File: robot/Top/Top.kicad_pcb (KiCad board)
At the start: 2 copper layers, 0 parts

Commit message: Top PCB
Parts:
- added C2: 10µ, Capacitors_SMD:C_1206, B.Cu at (134.2, 120.2)
- added C3: 1µ, Capacitors_SMD:C_1206, B.Cu at (172.0, 111.8)
- added C4: 1µ, Capacitors_SMD:C_1206, B.Cu at (172.0, 106.5)
- added C5: 1µ, Capacitors_SMD:C_1206, B.Cu at (172.0, 101.2)
- added C6: 4.7µ, Capacitors_SMD:C_1206, B.Cu at (165.0, 98.9)
- added C7: 4.7µ, Capacitors_SMD:C_1206, B.Cu at (168.4, 100.0)
- added D1: D_Schottky, Diodes_SMD:D_SOD-123, B.Cu at (150.5, 97.5)
- added D2: ORANGE, LEDs:LED_0603, B.Cu at (135.0, 109.8)
- added H1: BAT_MON, Custom:Mounting_Pad_Signal, B.Cu at (140.0, 94.5)
- added H10: GND, Custom:Mounting_Pad_Power, B.Cu at (129.2, 95.0)
- added H2: VBAT_SWITCH, Custom:Mounting_Pad_Power, B.Cu at (168.2, 95.0)
- added H3: OLED_~RES, Custom:Mounting_Pad_Signal, B.Cu at (164.5, 94.5)
- added H4: OLED_SCL, Custom:Mounting_Pad_Signal, B.Cu at (162.0, 94.5)
- added H5: OLED_SDA, Custom:Mounting_Pad_Signal, B.Cu at (159.5, 94.5)
- added H6: VBUS, Custom:Mounting_Pad_Power, B.Cu at (136.2, 95.0)
- added H7: 3V3, Custom:Mounting_Pad_Power, B.Cu at (132.8, 95.0)
- added H8: GND, Custom:Mounting_Pad_Power, B.Cu at (171.8, 95.0)
- added J1: Conn_01x02_Male, Custom:Conn_Bat, B.Cu at (131.0, 126.3)
- added R1: 100K, Resistors_SMD:R_1206, B.Cu at (129.6, 119.2)
- added R2: 100K, Resistors_SMD:R_1206, B.Cu at (129.6, 113.5)
- added R3: 1K, Resistors_SMD:R_1206, B.Cu at (130.7, 109.8)
- added R4: 5K, Resistors_SMD:R_1206, B.Cu at (138.9, 116.5)
- added R5: 330k, Resistors_SMD:R_1206, B.Cu at (165.1, 112.2)
- added SW1: SW_DPDT_x2, Custom:JS102011SAQN, B.Cu at (134.1, 103.8)
- added U2: MCP73831-2-OT, Package_TO_SOT_SMD:SOT-23-5, B.Cu at (134.2, 116.5)
- added U3: SSD1306, Custom:SSD1306_OLED, B.Cu at (165.2, 110.0)
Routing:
- net +3V3: track 0.00 -> 61.6 mm, vias 0 -> 2
- net /BAT_MON: track 0.00 -> 32.1 mm, vias 0 -> 2
- net +BATT: track 0.00 -> 29.3 mm, vias 0 -> 2
- net VBUS: track 0.00 -> 24.2 mm
- net /VBAT_SWITCH: track 0.00 -> 18.3 mm, vias 0 -> 2
- net Net-(D1-Pad2): track 0.00 -> 17.4 mm, vias 0 -> 2
- net /OLED_~RES: track 0.00 -> 14.9 mm
- net /OLED_SDA: track 0.00 -> 13.2 mm, vias 0 -> 2
- net /OLED_SCL: track 0.00 -> 12.6 mm, vias 0 -> 2
- net Net-(R5-Pad2): track 0.00 -> 12.5 mm, vias 0 -> 2
- net Net-(R3-Pad2): track 0.00 -> 12.2 mm
- net Net-(C6-Pad1): track 0.00 -> 9.27 mm, vias 0 -> 2
- net Net-(C3-Pad1): track 0.00 -> 8.20 mm
- net Net-(C4-Pad2): track 0.00 -> 8.15 mm
- net Net-(C3-Pad2): track 0.00 -> 7.21 mm
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- added copper zone on B.Cu, net GND
- added copper zone on F.Cu, net GND
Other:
- board outline added: 46 x 46 mm
- net class Power added: clearance 0.3, trace_width 0.5, via_dia 1, via_drill 0.5

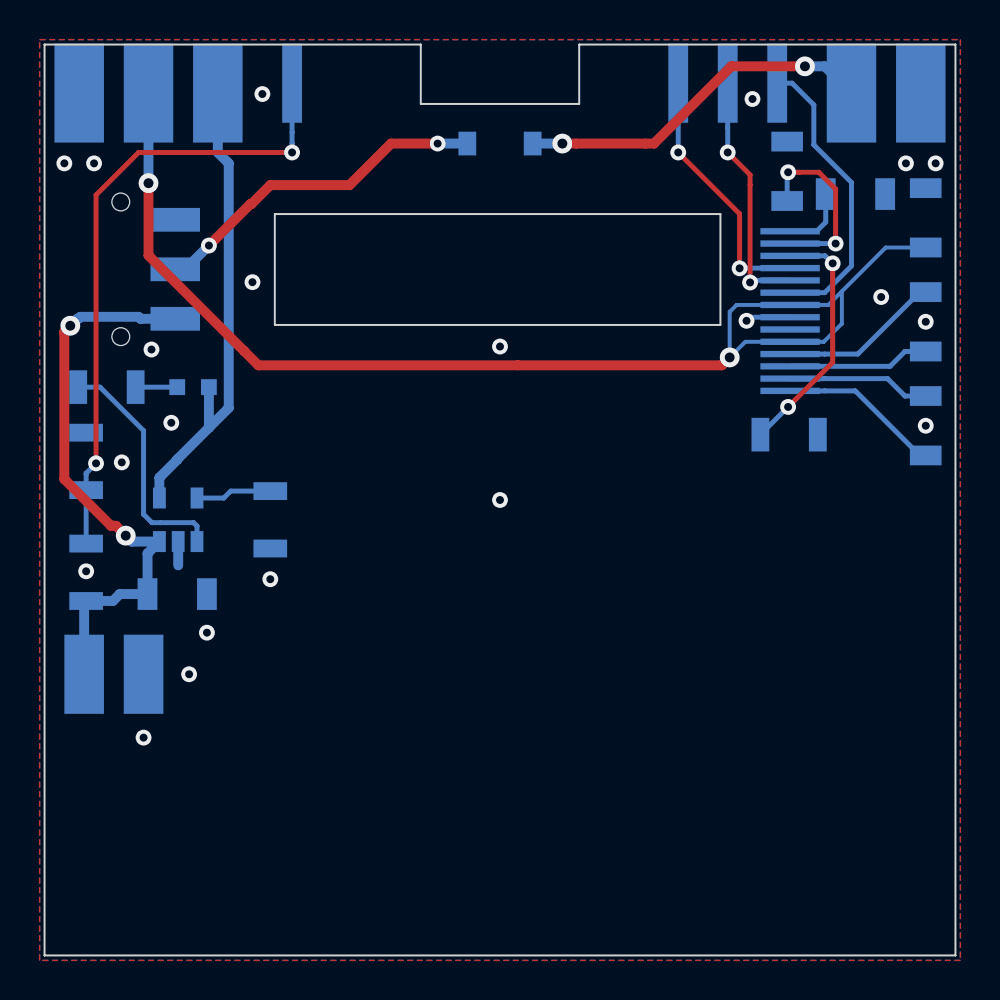
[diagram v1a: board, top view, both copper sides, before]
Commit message: Swap 3V3 and VBUS, Fix Cutout, small changes
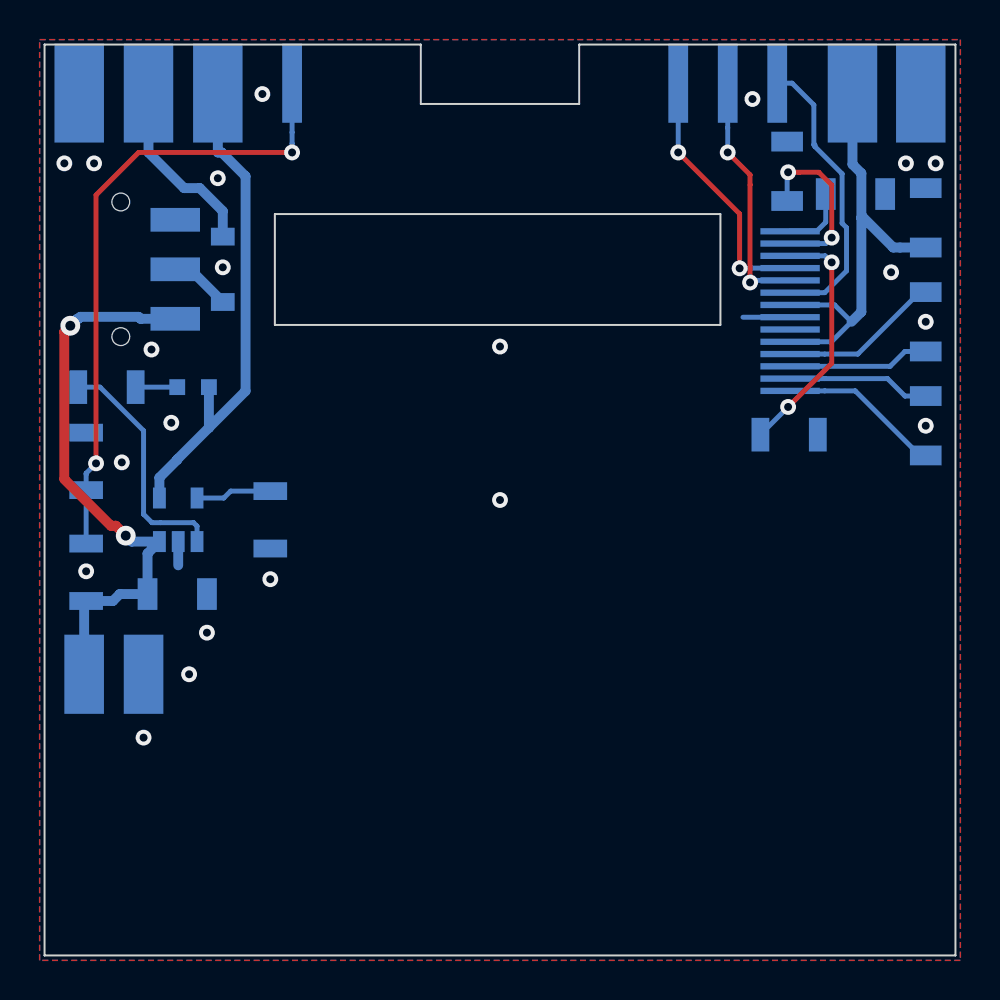
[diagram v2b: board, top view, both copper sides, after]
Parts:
- moved H7 35.6 mm to (168.3, 95.0)
- moved H2 35.5 mm to (132.8, 95.0)
- moved D1 15.4 mm to (136.5, 103.8), turned to 270 degrees
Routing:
- net +3V3: track 61.6 -> 22.8 mm, vias 2 -> 0
- net Net-(D1-Pad2): track 17.4 -> 4.03 mm, vias 2 -> 0
- net /VBAT_SWITCH: track 18.3 -> 9.27 mm, vias 2 -> 0
- net VBUS: track 24.2 -> 25.0 mm

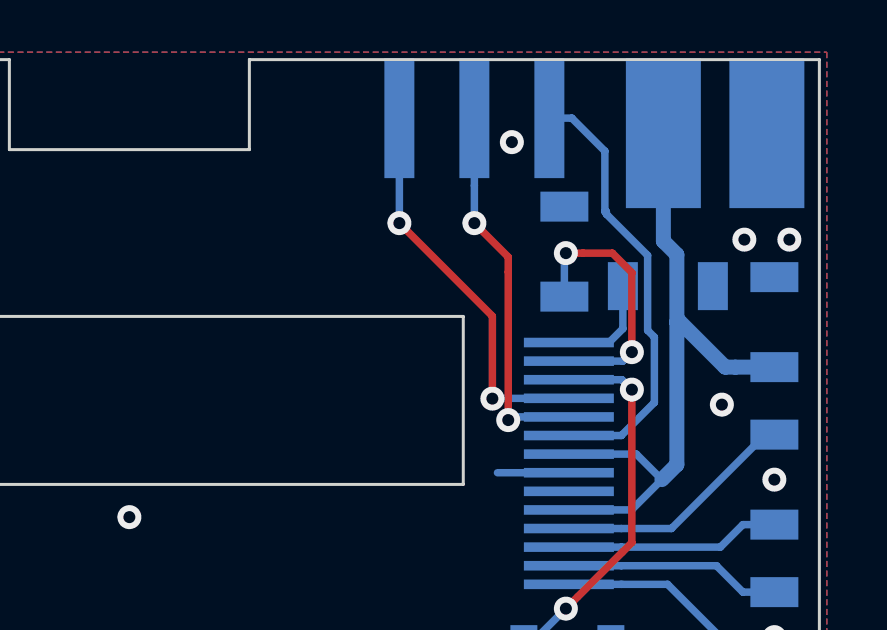
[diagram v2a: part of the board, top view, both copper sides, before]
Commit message: Silkscreen Top
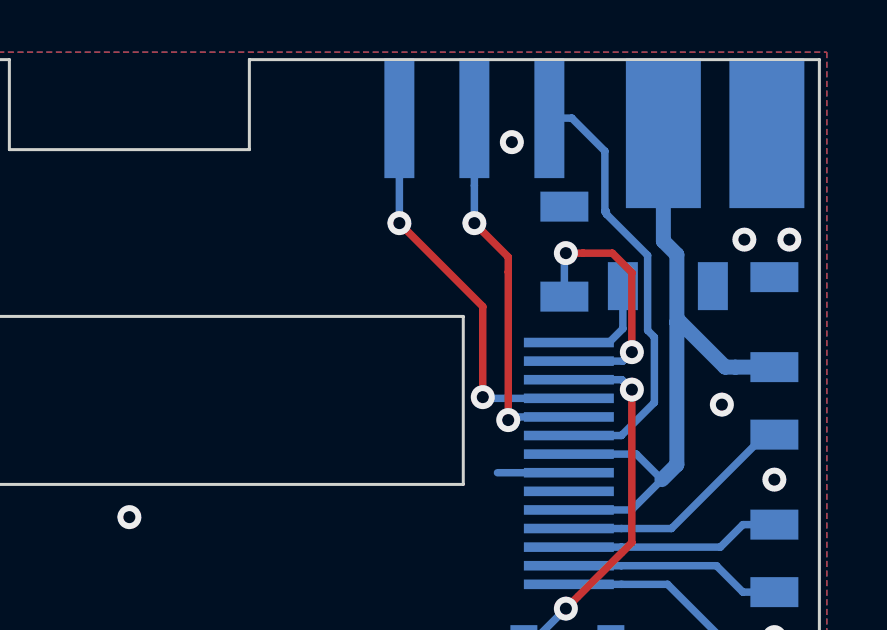
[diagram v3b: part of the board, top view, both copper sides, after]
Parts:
- H2: value VBAT_SWITCH -> VBS
- H3: value OLED_~RES -> ORST
- H4: value OLED_SCL -> OSCL
- H5: value OLED_SDA -> OSDA

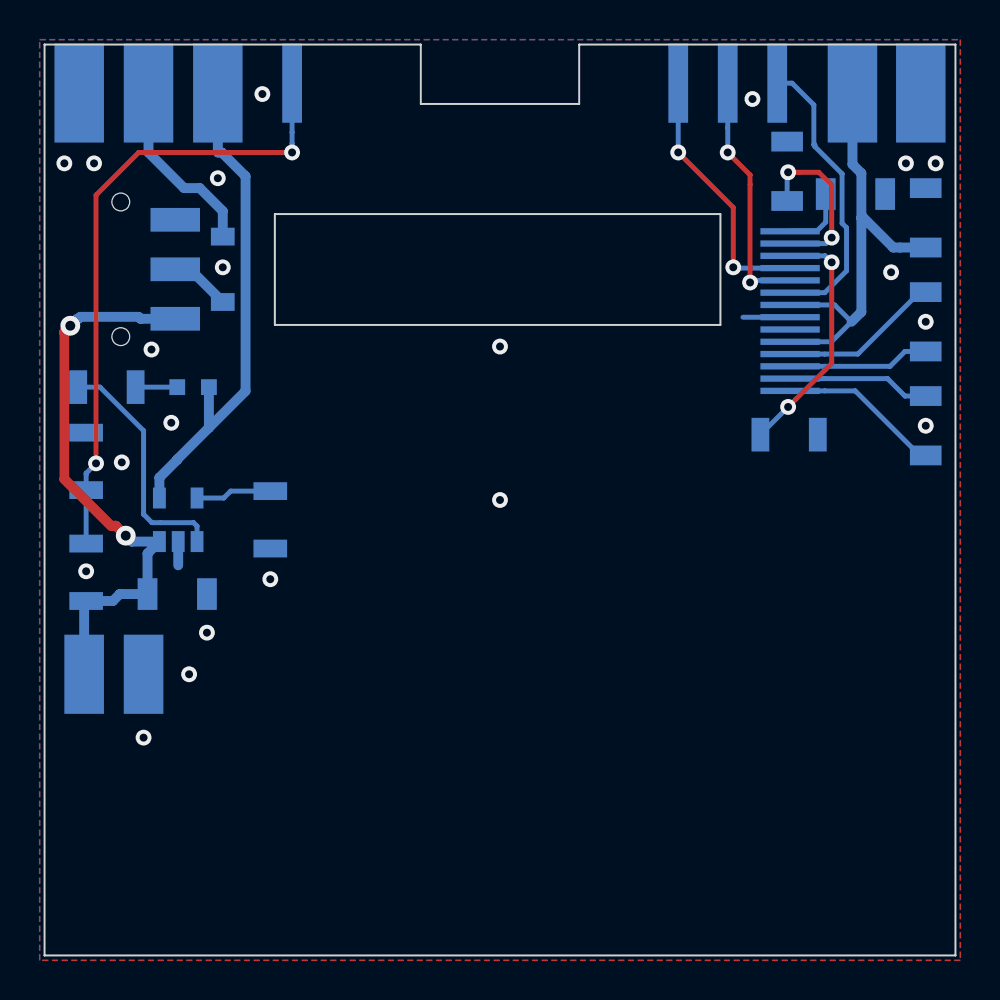
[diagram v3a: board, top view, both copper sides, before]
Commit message: Finish Top, remap OLED pins
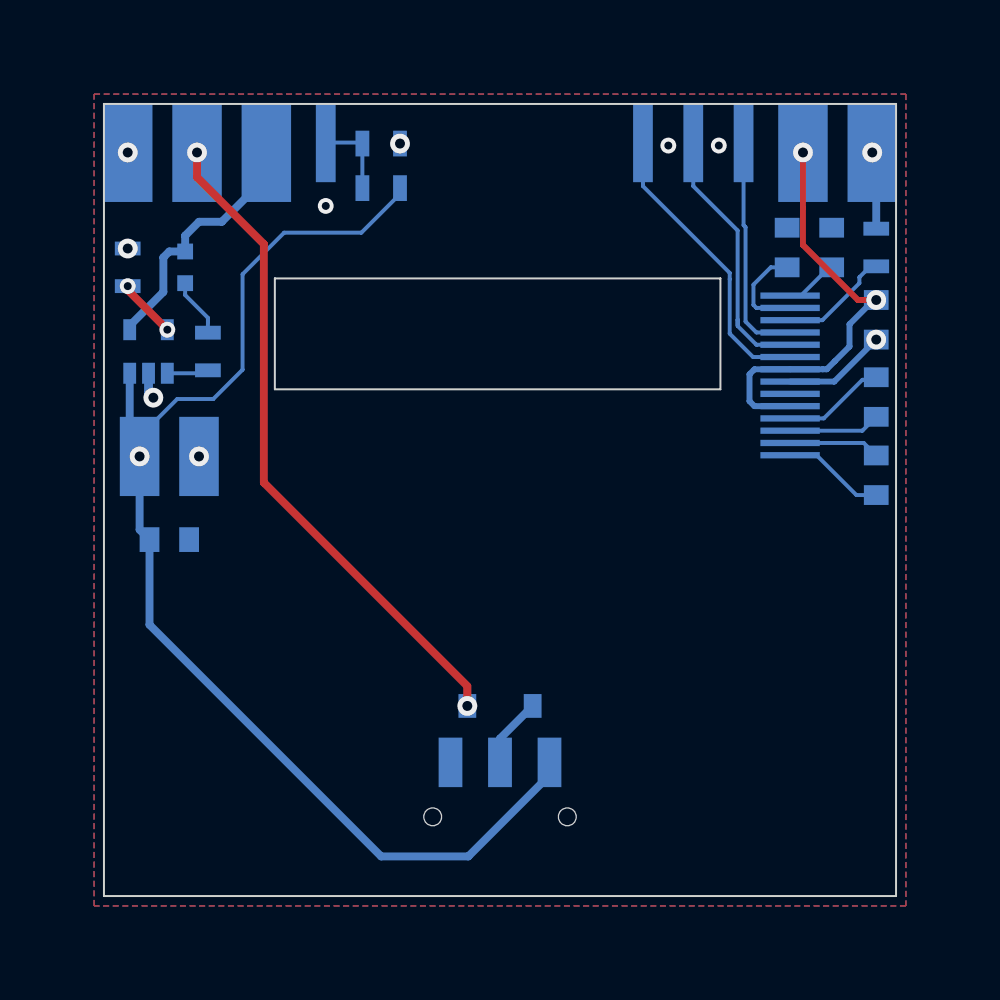
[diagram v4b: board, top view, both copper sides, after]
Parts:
- C2, C3, C4, C5, C6, C7: footprint Capacitors_SMD:C_1206 -> Capacitors_SMD:C_0805
- H1: value BAT_MON -> BTMN
- R1, R2, R3, R4, R5: footprint Resistors_SMD:R_1206 -> Resistors_SMD:R_0805
- moved SW1 29.8 mm to (150.5, 128.8), turned to 180 degrees
- moved D1 26.1 mm to (150.5, 125.9), turned to 0 degrees
- moved R1 24.5 mm to (144.5, 99.8), turned to 180 degrees
- moved R2 21.9 mm to (144.5, 97.5), turned to 0 degrees
- moved R4 14.6 mm to (131.7, 103.8), turned to 90 degrees
- moved J1 11.4 mm to (133.8, 115.3)
- moved R5 10.4 mm to (169.5, 102.8), turned to 270 degrees
- moved U2 8.63 mm to (132.8, 108.0)
- moved H3 7.41 mm to (157.7, 97.5)
- moved D2 6.06 mm to (134.6, 103.8), turned to 90 degrees
- moved C5 5.72 mm to (169.5, 106.4), turned to 270 degrees
- moved R3 5.41 mm to (135.8, 108.0), turned to 270 degrees
- moved C4 4.55 mm to (169.5, 110.3)
- moved H5 4.46 mm to (162.8, 97.5)
- moved H7 3.91 mm to (165.8, 98.0)
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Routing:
- net +BATT: track 29.3 -> 62.9 mm, vias 2 -> 1
- net /BAT_MON: track 32.1 -> 4.12 mm, vias 2 -> 0
- net /VBAT_SWITCH: track 9.27 -> 33.6 mm, vias 0 -> 2
- net VBUS: track 25.0 -> 14.7 mm
- net Net-(R3-Pad2): track 12.2 -> 2.11 mm
- net GND: track 3.58 -> 11.6 mm, vias 21 -> 10
- net Net-(R5-Pad2): track 12.4 -> 5.65 mm, vias 2 -> 0
- net Net-(C6-Pad1): track 8.81 -> 5.00 mm, vias 2 -> 0
- net Net-(C3-Pad1): track 8.20 -> 5.18 mm
- net Net-(C4-Pad2): track 8.15 -> 5.21 mm
- net Net-(C3-Pad2): track 7.21 -> 4.61 mm
- net Net-(C4-Pad1): track 7.16 -> 4.64 mm
- net /OLED_~RES: track 14.7 -> 16.5 mm
- net /OLED_SDA: track 13.4 -> 11.6 mm, vias 2 -> 0
- net +3V3: track 22.8 -> 21.7 mm, vias 0 -> 2
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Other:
- board size 46 x 46 mm -> 40 x 40 mm
- net class Default: trace_width 0.25 -> 0.2
- net class Power: trace_width 0.5 -> 0.4

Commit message: Small fixes, step files
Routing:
- net +BATT: track 62.9 -> 62.3 mm, vias 1 -> 0
- net /VBAT_SWITCH: track 33.6 -> 34.1 mm, vias 2 -> 3
- net GND: vias 10 -> 11
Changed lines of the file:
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@@
     (thickness 1.6)
     (drawings 13)
-    (tracks 130)
+    (tracks 137)
     (zones 0)
     (modules 26)
@@
   (via (at 161.55 97.6) (size 0.8) (drill 0.4) (layers F.Cu B.Cu) (net 1))
   (via (at 141.7 100.65) (size 0.8) (drill 0.4) (layers F.Cu B.Cu) (net 1))
+  (via (at 150.5 115.5) (size 1) (drill 0.5) (layers F.Cu B.Cu) (net 1))
   (segment (start 145.45 100.05) (end 145.45 99.75) (width 0.2) (layer B.Cu) (net 2))
   (segment (start 131.8 112.8) (end 132.3 113.3) (width 0.4) (layer B.Cu) (net 2))
@@
   (segment (start 144.5 133.5) (end 148.9 133.5) (width 0.4) (layer B.Cu) (net 2))
   (segment (start 132.3 113.3) (end 132.3 112.3) (width 0.2) (layer B.Cu) (net 2))
-  (segment (start 132.3 112.3) (end 134.2 110.4) (width 0.2) (layer B.Cu) (net 2))
-  (segment (start 137.5 104.1) (end 139.6 102) (width 0.2) (layer B.Cu) (net 2))
-  (segment (start 134.2 110.4) (end 136.020002 110.4) (width 0.2) (layer B.Cu) (net 2))
-  (segment (start 136.020002 110.4) (end 137.5 108.920002) (width 0.2) (layer B.Cu) (net 2))
-  (segment (start 137.5 108.920002) (end 137.5 104.1) (width 0.2) (layer B.Cu) (net 2))
-  (via (at 132.3 113.3) (size 1) (drill 0.5) (layers F.Cu B.Cu) (net 2))
-  (segment (start 139.6 102) (end 143.5 102) (width 0.2) (layer B.Cu) (net 2))
   (segment (start 143.5 102) (end 145.45 100.05) (width 0.2) (layer B.Cu) (net 2))
+  (segment (start 143.5 102) (end 137.95 102) (width 0.2) (layer B.Cu) (net 2))
+  (segment (start 137.95 102) (end 136.85001 103.09999) (width 0.2) (layer B.Cu) (net 2))
+  (segment (start 136.85001 107.669992) (end 136.420002 108.1) (width 0.2) (layer B.Cu) (net 2))
+  (segment (start 136.85001 103.09999) (end 136.85001 107.669992) (width 0.2) (layer B.Cu) (net 2))
+  (segment (start 131.8 108.37) (end 131.8 109.1) (width 0.2) (layer B.Cu) (net 2))
+  (segment (start 132.07 108.1) (end 131.8 108.37) (width 0.2) (layer B.Cu) (net 2))
+  (segment (start 136.420002 108.1) (end 132.07 108.1) (width 0.2) (layer B.Cu) (net 2))
   (segment (start 168.5 115.25) (end 169.5 115.25) (width 0.2) (layer B.Cu) (net 3))
   (segment (start 165.15 113.24) (end 166.49 113.24) (width 0.2) (layer B.Cu) (net 3))
@@
   (segment (start 168.87 112.62) (end 169.5 113.25) (width 0.2) (layer B.Cu) (net 4))
   (segment (start 165.15 112.62) (end 168.87 112.62) (width 0.2) (layer B.Cu) (net 4))
-  (segment (start 166.85 111.38) (end 168.8 109.43) (width 0.2) (layer B.Cu) (net 5))
-  (segment (start 165.15 111.38) (end 166.85 111.38) (width 0.2) (layer B.Cu) (net 5))
-  (segment (start 169.37 109.43) (end 169.5 109.3) (width 0.2) (layer B.Cu) (net 5))
-  (segment (start 168.8 109.43) (end 169.37 109.43) (width 0.2) (layer B.Cu) (net 5))
+  (segment (start 166.85 111.38) (end 165.15 111.38) (width 0.2) (layer B.Cu) (net 5))
+  (segment (start 167.25 110.98) (end 166.85 111.38) (width 0.2) (layer B.Cu) (net 5))
+  (segment (start 167.25 110.5) (end 167.25 110.98) (width 0.2) (layer B.Cu) (net 5))
+  (segment (start 168.32 109.43) (end 167.25 110.5) (width 0.2) (layer B.Cu) (net 5))
+  (segment (start 169.5 109.3) (end 169.37 109.43) (width 0.2) (layer B.Cu) (net 5))
+  (segment (start 169.37 109.43) (end 168.32 109.43) (width 0.2) (layer B.Cu) (net 5))
   (segment (start 168.8 112) (end 169.5 111.3) (width 0.2) (layer B.Cu) (net 6))
   (segment (start 165.15 112) (end 168.8 112) (width 0.2) (layer B.Cu) (net 6))
@@
   (via (at 135.2 97.95) (size 1) (drill 0.5) (layers F.Cu B.Cu) (net 10))
   (via (at 148.85 125.9) (size 1) (drill 0.5) (layers F.Cu B.Cu) (net 10))
-  (segment (start 148.85 125.9) (end 148.85 124.9) (width 0.4) (layer F.Cu) (net 10))
-  (segment (start 138.575 102.575) (end 138.575 114.625) (width 0.4) (layer F.Cu) (net 10))
-  (segment (start 135.2 99.2) (end 138.575 102.575) (width 0.4) (layer F.Cu) (net 10))
   (segment (start 135.2 97.95) (end 135.2 99.2) (width 0.4) (layer F.Cu) (net 10))
-  (segment (start 148.85 124.9) (end 138.575 114.625) (width 0.4) (layer F.Cu) (net 10))
+  (segment (start 135.2 99.2) (end 137.1 101.1) (width 0.4) (layer F.Cu) (net 10))
+  (via (at 137.55 110.9) (size 1) (drill 0.5) (layers F.Cu B.Cu) (net 10))
+  (segment (start 137.1 110.45) (end 137.55 110.9) (width 0.4) (layer F.Cu) (net 10))
+  (segment (start 137.1 110.35) (end 137.1 110.45) (width 0.4) (layer F.Cu) (net 10))
+  (segment (start 137.1 101.1) (end 137.1 110.35) (width 0.4) (layer F.Cu) (net 10))
+  (segment (start 148 125.9) (end 148.85 125.9) (width 0.4) (layer B.Cu) (net 10))
+  (segment (start 137.55 115.45) (end 148 125.9) (width 0.4) (layer B.Cu) (net 10))
+  (segment (start 137.55 110.9) (end 137.55 115.45) (width 0.4) (layer B.Cu) (net 10))
   (segment (start 150.5 127.55) (end 152.15 125.9) (width 0.4) (layer B.Cu) (net 11))
   (segment (start 150.5 128.75) (end 150.5 127.55) (width 0.4) (layer B.Cu) (net 11))
@@
   (segment (start 133.5 103.25) (end 133.8 102.95) (width 0.4) (layer B.Cu) (net 12))
   (segment (start 133.5 104.995) (end 133.5 103.25) (width 0.4) (layer B.Cu) (net 12))
-  (segment (start 138.7 99.65) (end 138.7 97.95) (width 0.4) (layer B.Cu) (net 12))
   (segment (start 138.7 97.95) (end 138.7 99.2) (width 0.4) (layer B.Cu) (net 12))
   (segment (start 135.3 101.45) (end 136.45 101.45) (width 0.4) (layer B.Cu) (net 12))
@@
   (segment (start 134.6 102.95) (end 134.6 102.15) (width 0.4) (layer B.Cu) (net 12))
   (segment (start 138.7 99.2) (end 136.45 101.45) (width 0.4) (layer B.Cu) (net 12))
+  (segment (start 138.7 99.65) (end 138.7 97.95) (width 0.4) (layer B.Cu) (net 12))
   (segment (start 135.75 106.5) (end 135.75 107.05) (width 0.2) (layer B.Cu) (net 13))
   (segment (start 135.75 106.3) (end 135.75 106.5) (width 0.2) (layer B.Cu) (net 13))
